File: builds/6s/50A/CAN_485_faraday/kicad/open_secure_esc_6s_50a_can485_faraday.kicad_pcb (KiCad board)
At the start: 4 copper layers, 32 x 60.1 mm, 59 parts, among them J1 SolderPad_1x04_SMD_P1.27mm_Pr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, J2 SolderPad_1x02_SMD_P2.54mm, J3 SolderPad_1x02_SMD_P2.54mm, J4A SolderWirePad_1x01_SMD_5x10mm, J4B SolderWirePad_1x01_SMD_5x10mm, J4C SolderWirePad_1x01_SMD_5x10mm, J5A SolderWire-6sqmm_1x01_D3.5mm_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, J5B SolderWire-6sqmm_1x01_D3.5mm_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, Q1 Toshiba_2-5W1A_SOP-Advance-N_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, Q2 Toshiba_2-5W1A_SOP-Advance-N_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, Q3 Toshiba_2-5W1A_SOP-Advance-N_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, Q4 Toshiba_2-5W1A_SOP-Advance-N_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, Q5 Toshiba_2-5W1A_SOP-Advance-N_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, Q6 Toshiba_2-5W1A_SOP-Advance-N_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, U1 LQFP-64_10x10mm_P0.5mm, U2 Infineon_PG-USON-10-2-4_3x3mm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, U3 SOIC-20W_7.5x12.8mm_P1.27mm, U4 SOIC-20W_7.5x12.8mm_P1.27mm, U5 TI_RTA0040B_WQFN-40_6x6mm_P0.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, U6 SOIC-8_3.9x4.9mm_P1.27mm, U7 SOIC-8_3.9x4.9mm_P1.27mm, U8 SOIC-8_3.9x4.9mm_P1.27mm

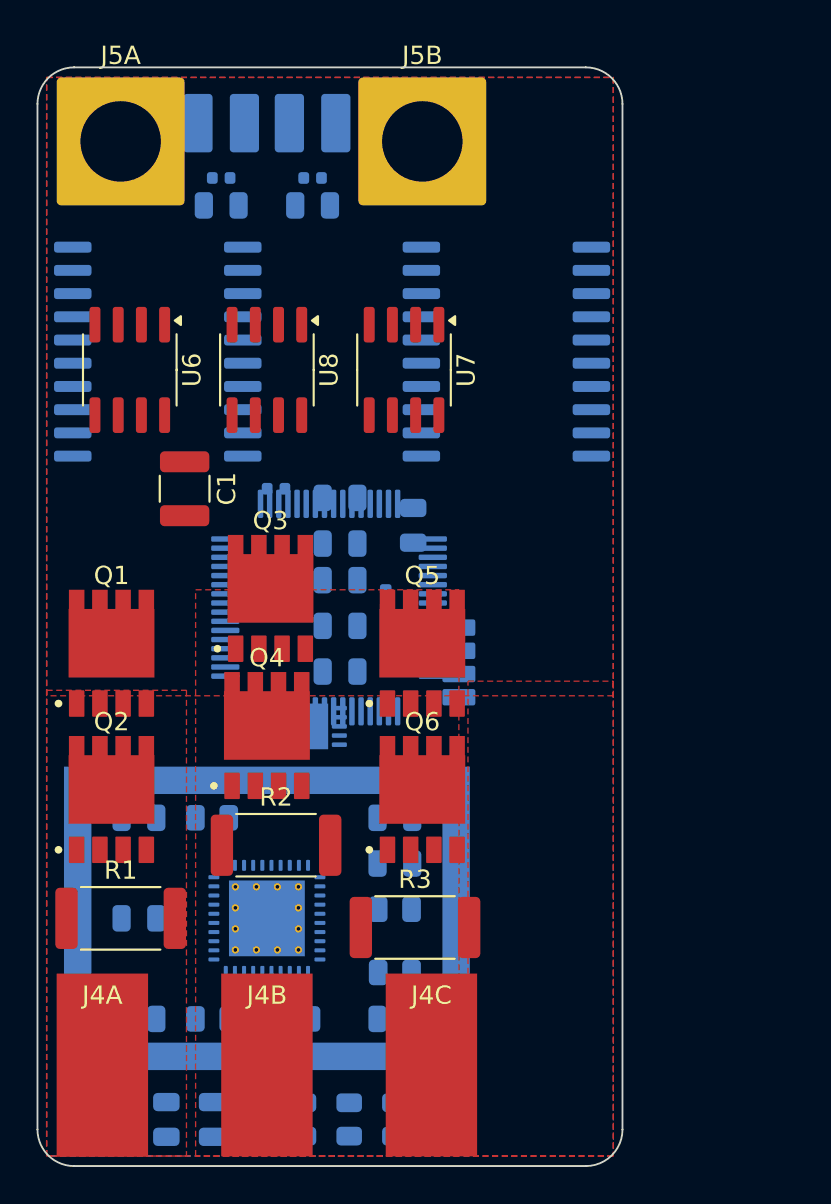
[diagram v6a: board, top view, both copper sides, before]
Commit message: Clean up placement rows and columns, measured rather than eyeballed
The owner asked for row/column cleanup optimising electrical quality,
scriptability and visual order. Built a measurement harness first --
tools/score_placement.py -- so each change could be kept or reverted on a
number. Four experiments, serial, logged to disk after each.

                        baseline    final
  DRC electrical             402        0
  on 0.5 mm grid           81.4%   100.0%
  distinct rows               34       30
  distinct columns            28       23
  sharing a row/column     69.5%    78.0%
  isolated lead max       9.94mm   8.73mm   ([9] p.17 caps this at 10)
  creepage min            2.74mm   3.98mm   (needs 7.5 -- still short)

EXPERIMENT 1 (kept): refill zones. 402 -> 0 electrical violations without
moving anything. All 210 clearance, 183 solder-mask-bridge and 9
hole-clearance findings were copper sitting where parts no longer are. This is
the third time this session a frightening violation count turned out to be
stale fill; the harness now runs a refill implicitly by measuring after one.

EXPERIMENT 2 (reverted): move FB4 between the pins it bridges. Produced the
best isolated lead of the run, 6.75 mm, and collided with C16. The outboard
strip beside U4 is single-file -- a part can only go in the gaps between
existing ones, not at an arbitrary y.

EXPERIMENT 3 (kept): pull the three outliers into the two support columns the
owner had already established at x=1.60 and x=30.60. Took two corrections:
C12 and C18 were at rot 0/180 (2.90 mm wide) while every other part in those
columns is at rot 90 (1.44 mm), so moving them in at their own rotation pushed
copper past the 0.55 mm edge window; and C12 then overlapped FB1 by 0.05 mm.
Column membership is rotation plus position, not position alone.

EXPERIMENT 4 (kept): snap all 59 footprints to a 0.5 mm grid. 13 moved, the
largest by 0.25 mm, and that alone collapsed 4 rows and 3 columns -- parts
within a quarter millime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
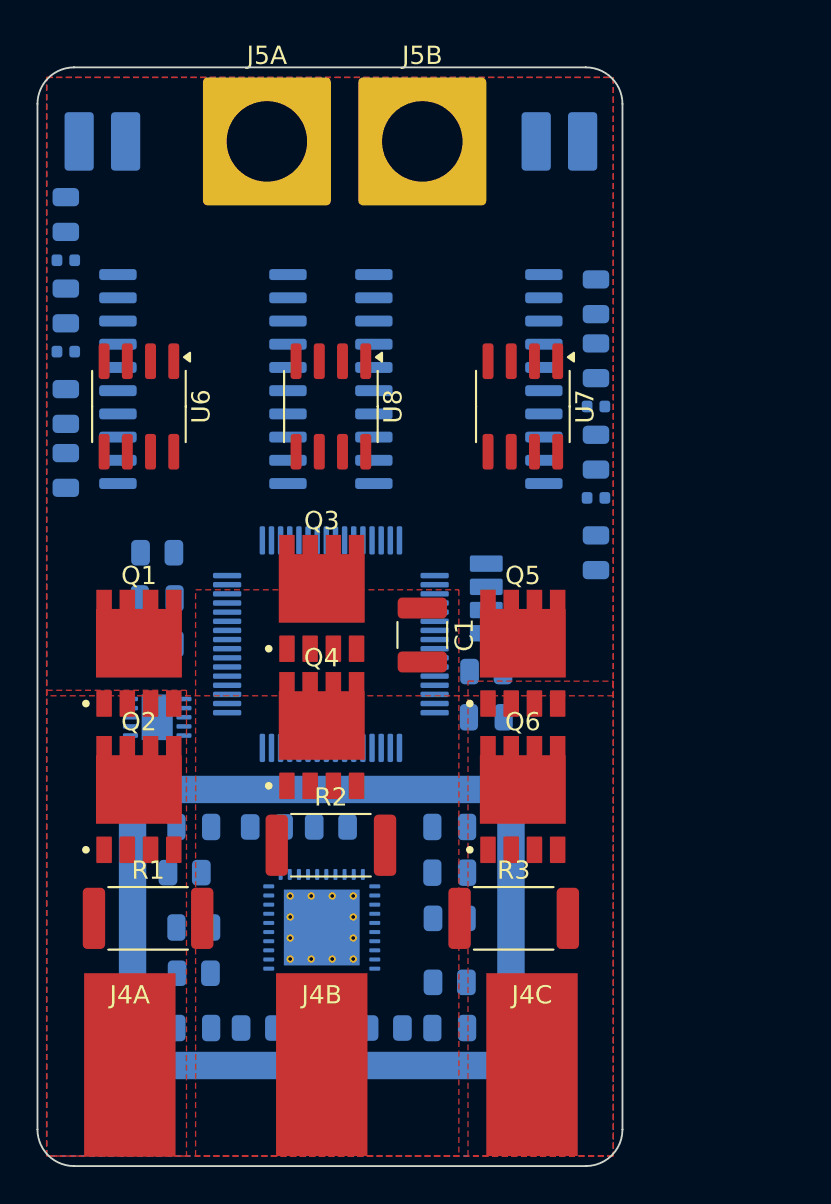
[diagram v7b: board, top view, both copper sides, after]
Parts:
- moved R12 31.6 mm to (44.5, 53.0), turned to 0 degrees
- moved R7 31.5 mm to (26.5, 46.5), turned to 180 degrees
- moved C10 31.1 mm to (44.5, 55.5), turned to 0 degrees
- moved C4 28.7 mm to (26.5, 49.0), turned to 180 degrees
- moved C3 26.0 mm to (26.5, 51.5), turned to 180 degrees
- moved C11 22.5 mm to (21.5, 33.0), turned to 90 degrees
- moved C12 21.6 mm to (21.5, 28.0), turned to 90 degrees
- moved C15 19.4 mm to (50.5, 32.5), turned to 90 degrees
- moved C16 17.7 mm to (50.5, 36.0), turned to 90 degrees
- moved FB4 17.5 mm to (50.5, 43.5), turned to 0 degrees
- moved C17 16.9 mm to (50.5, 41.0), turned to 90 degrees
- moved FB2 16.5 mm to (21.5, 35.5)
- moved R14 16.2 mm to (28.0, 64.0), turned to 180 degrees
- moved C14 16.2 mm to (21.5, 42.0), turned to -90 degrees
- moved R6 16.1 mm to (36.0, 61.5), turned to 180 degrees
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
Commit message: Owner's U1/U5 swap clears creepage for the first time: 3.98 -> 7.68 mm
Measured with tools/score_placement.py against the previous best.

                    before     after
  creepage min      3.98mm    7.68mm   PASSES (needs 7.5)
  gate loop max    22.32mm   16.83mm
  commutation      17.41mm   17.97mm
  DRC electrical         0         0
  distinct rows         30        37
  alignment          78.0%     69.5%

The swap moved U5 into the shield centred under the FET array (y 33.10 in a
23.62..44.08 span) and moved U1 clear to y 49.10, which is what opened the
isolation room. U2 also went inside the shield. Verified the README's
shortest-gate-loop constraint still holds -- U5 is under the FETs, and the
5.5 mm gate-loop improvement confirms it.

Creepage margin is thin: 7.68 against 7.5, i.e. 0.18 mm, binding on
C18.1 <-> C8.1. Worth widening before fab.

THREE FAILED ATTEMPTS TO RECOVER THE LOST ROW ALIGNMENT, all reverted:

  exp5  consolidate near-miss rows/columns at 0.75 mm tolerance.
        Regularity gains were the largest of the whole run -- rows 37->24,
        columns 24->14, alignment 69.5%->89.8% -- but creepage fell to
        7.03 mm and DRC went to 28. Both constraints broken; reverted.
  exp6  same at 0.30 mm tolerance. Consolidated nothing: every footprint is
        already on the 0.5 mm grid, so no two distinct coordinates are closer
        than 0.5 mm and no cluster can form below that.
  exp7  restrict consolidation to the 35 parts more than 9 mm from any
        isolated conductor, so creepage cannot move. Creepage did hold at
        7.68, and rows went 37->30 with alignment to 80.5% -- but DRC went to
        20 on ordinary clearance. Reverted.

THE FINDING FROM THOSE THREE: this board is at a local optimum. Because every
part already sits on the 0.5 mm grid, any further row or column consolidation
requires moving a part at least 0.5 mm, and at this density 0.5 mm is enough
to break a clearance somewhere. Row alignment beyond this point i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
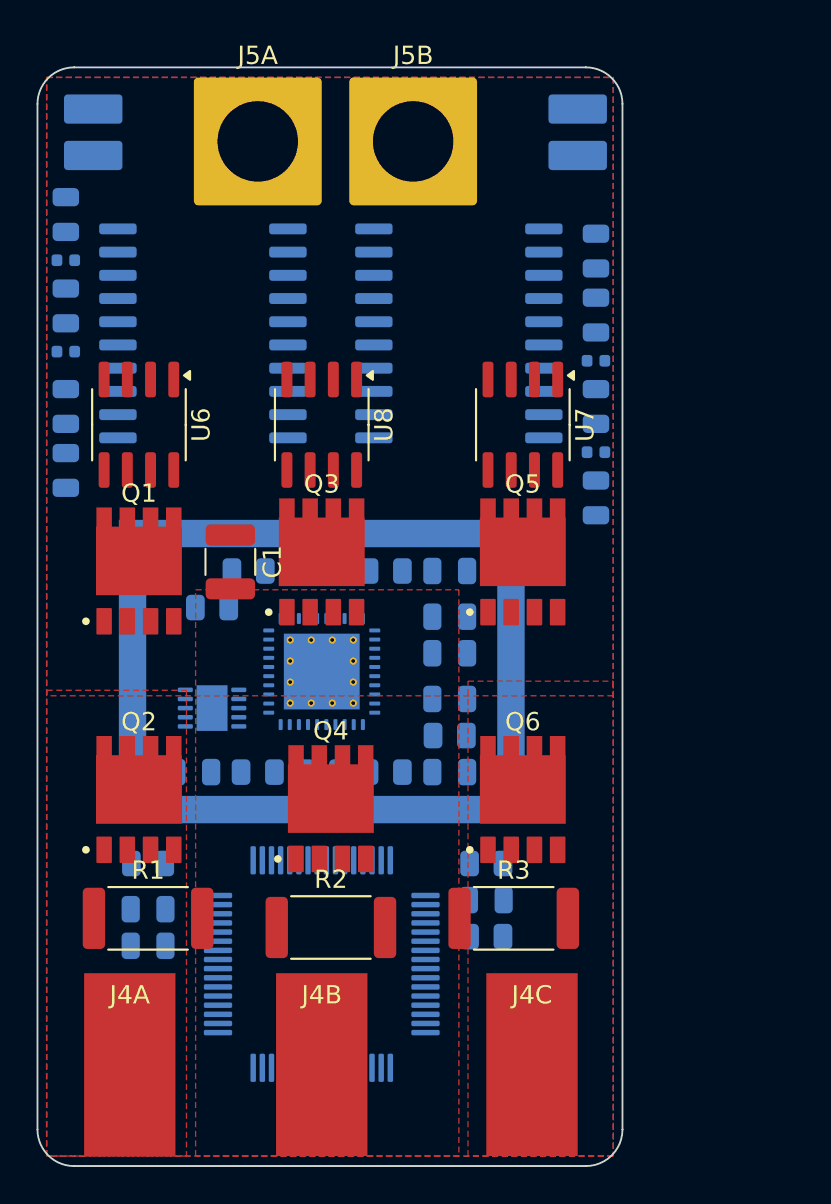
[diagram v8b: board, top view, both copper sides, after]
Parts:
- moved J1 29.9 mm to (26.0, 72.5), turned to -90 degrees
- moved R11 22.2 mm to (31.5, 47.5)
- moved C6 18.8 mm to (42.5, 54.5)
- moved U1 17.5 mm to (35.5, 69.0)
- moved C4 17.0 mm to (26.0, 66.0)
- moved R7 17.0 mm to (26.0, 63.5)
- moved C5 16.9 mm to (42.5, 52.0)
- moved C3 16.5 mm to (26.0, 68.0)
- moved R14 14.6 mm to (29.5, 49.5)
- moved R6 14.3 mm to (39.0, 47.5)
- moved R9 14.2 mm to (35.0, 47.5)
- moved C2 14.0 mm to (42.5, 50.0)
- moved C7 14.0 mm to (42.5, 58.5)
- moved C8 14.0 mm to (42.5, 47.5)
- moved C9 14.0 mm to (28.5, 58.5)
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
